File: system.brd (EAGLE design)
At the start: 52.4 x 77 mm, 122 parts, among them IC1 TPS7B8650BQDDARQ1, J1 OLED, J2 163-179PH-EX, J3 AD2, J4 MCU, SW1 1825910-6, SW2 1825910-6, SW3 1825910-6, U1 ATMEGA328PB-AU, Y1 ABL-16.000MHZ-B2

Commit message: routing
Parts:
- removed J3: AD2, RS1-02-G:CONN_RS1-02-G_ADM
- removed LDO:J1: RS1-02-G, RS1-02-G:CONN_RS1-02-G_ADM
- removed SW2, SW3: 1825910-6, 1825910-6:SW_1825910-6-4
- added 5V_BACKUP: 5010, 5010:5010
- added AD2_BG: AD2_BG, RS1-02-G:CONN_RS1-02-G_ADM
- added LDO:AD2_5V: RS1-02-G, RS1-02-G:CONN_RS1-02-G_ADM
- added SW_MCU_RST, SW_MISC1: 1825910-6, 1825910-6:SW_1825910-6-4
- added U$1, U$2, U$3, U$4: (no value), SparkFun-Hardware:STAND-OFF
- moved V_TH 61.8 mm to (48.8, 27.1)
- moved RST_ADC 48.8 mm to (42.3, -5.71)
- moved TP10 47.7 mm to (28.6, -6.10)
- moved SDA 40.1 mm to (22.9, -6.22)
- moved ADC:C1 38.1 mm to (45.2, -1.91)
- moved R18 38.0 mm to (49.1, -0.76)
- moved 1.5V 34.9 mm to (10.7, 33.1)
- moved C6 34.7 mm to (50.7, 2.03)
- moved ADC:R2 33.2 mm to (44.7, 2.29)
- moved L1 30.8 mm to (13.2, -3.56), flipped to the bottom
- moved MCU_RST 29.5 mm to (10.7, 27.1)
- moved ADC:IC1 29.3 mm to (39.2, -1.14)
- moved 5V 28.6 mm to (16.8, 42.3)
- moved 2.5V 28.2 mm to (17.1, 33.1)
- moved ADC:C2 26.9 mm to (33.4, 10.9)
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- renumbered SW1 to SW_START
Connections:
- net 0: now also AD2_BG.1, LDO:AD2_5V.2, SW_MCU_RST.1, SW_MISC1.1; no longer J3.1, LDO:J1.2, SW2.1, SW3.1
- net LDO:N$3: now also LDO:AD2_5V.1; no longer LDO:J1.1
- net MCU_RST: now also SW_MCU_RST.3; no longer SW3.3
- net N$11: now also AD2_BG.2; no longer J3.2
- net N$19: now also SW_MCU_RST.4, SW_MISC1.4; no longer SW2.4, SW3.4
- net PB_MISC1: now also SW_MISC1.3; no longer SW2.3
- net VS_5V_BACKUP: now also 5V_BACKUP.1
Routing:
- net VS_5V_OUT: track 31.6 -> 98.4 mm, vias 2 -> 4
- net MCU_RST: track 0.00 -> 46.5 mm, vias 0 -> 2
- net PB_START: track 0.00 -> 42.0 mm
- net BG:N$4: track 37.1 -> 11.0 mm, vias 2 -> 1
- net N$4: track 0.00 -> 25.3 mm
- net PB_MISC1: track 0.00 -> 23.2 mm
- net ADC:N$2: track 23.2 -> 0.00 mm, vias 2 -> 0
- net VS_1.5V_OUT: track 7.51 -> 25.8 mm, vias 0 -> 1
- net BK:N$2: track 32.8 -> 14.5 mm, vias 1 -> 0
- net SDA: track 0.00 -> 17.4 mm, vias 0 -> 2
- net ADC:N$4: track 17.0 -> 0.00 mm
- net V_SIG: track 16.9 -> 0.23 mm
- net N$5: track 16.4 -> 0.00 mm, vias 2 -> 0
- net MOSI_MCU: track 0.00 -> 13.9 mm
- net VS_9V: track 0.08 -> 12.9 mm
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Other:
- board size 52.4 x 77 mm -> 54.3 x 78.5 mm
- board text removed: "5V"
- board text removed: "BUCK IC"
- board text removed: "gnd"

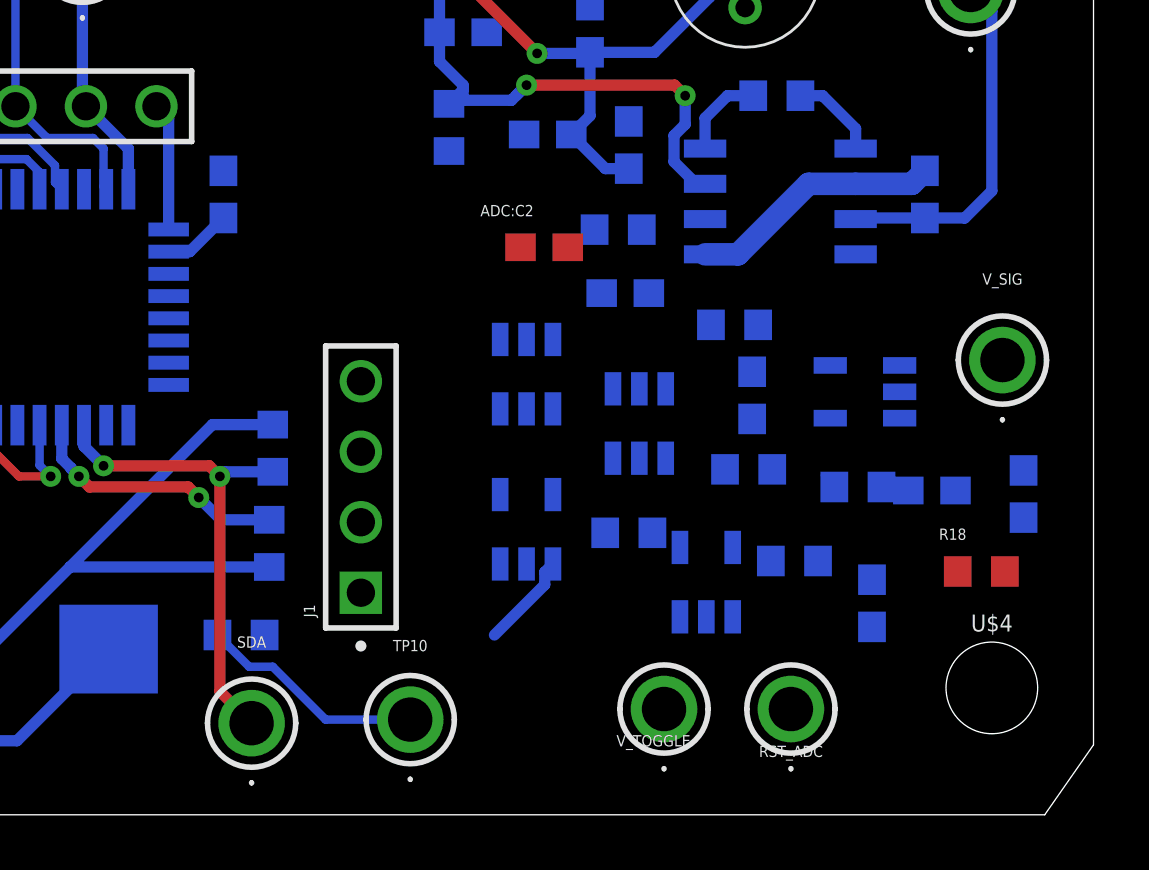
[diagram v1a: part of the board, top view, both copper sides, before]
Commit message: Rerouting ADC and AF
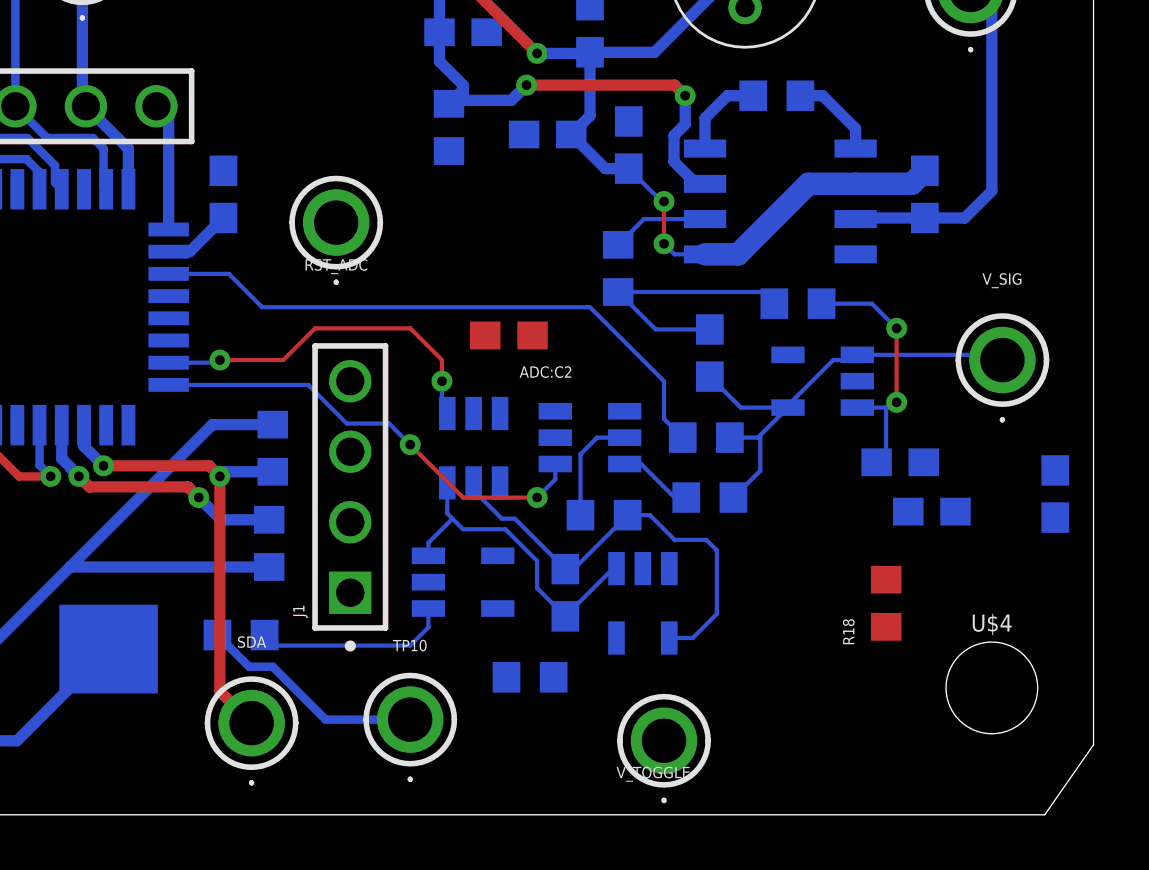
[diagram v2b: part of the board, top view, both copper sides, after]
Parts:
- moved RST_ADC 24.0 mm to (25.9, 11.8)
- moved ADC:R2 13.7 mm to (32.9, -4.57)
- moved AF:C8 11.6 mm to (46.2, 3.17)
- moved ADC:C1 11.1 mm to (34.2, -1.52)
- moved R16 3.81 mm to (39.4, 1.91)
- moved R18 3.61 mm to (45.7, -1.91), turned to 90 degrees
- moved ADC:C2 3.42 mm to (32.1, 7.75), turned to 0 degrees
- moved ADC:IC4 3.28 mm to (30.9, 3.68)
- moved ADC:IC2 2.98 mm to (30.5, -1.14), turned to 180 degrees
- moved AF:R5 2.41 mm to (42.5, 8.89)
- moved ADC:IC1 2.41 mm to (37.0, -1.91), turned to 270 degrees
- moved AF:C7 2.16 mm to (39.4, 7.11)
- moved R19 1.91 mm to (39.2, 4.06)
- moved ADC:IC5 1.85 mm to (35.1, 4.06), turned to 180 degrees
- moved AF:IC2 1.57 mm to (43.4, 6.10)
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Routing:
- net V_SIG_ADC: track 0.13 -> 21.9 mm
- net V_SIG: track 0.23 -> 17.1 mm
- net V_TOGGLE: track 0.00 -> 16.4 mm, vias 0 -> 2
- net ADC:N$4: track 0.00 -> 15.9 mm
- net RST_ADC: track 0.00 -> 12.8 mm, vias 0 -> 2
- net ADC:N$2: track 0.00 -> 11.7 mm
- net AF:N$6: track 0.21 -> 9.66 mm
- net AF:N$7: track 0.00 -> 9.35 mm, vias 0 -> 2
- net VS_2.5V_OUT: track 53.4 -> 58.3 mm, vias 3 -> 5
- net ADC:N$1: track 0.00 -> 4.04 mm
- net N$14: track 4.03 -> 7.61 mm
- net AF:N$3: track 0.54 -> 3.75 mm
- net N$2: track 0.00 -> 2.72 mm
- net N$6: track 0.54 -> 0.00 mm

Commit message: Update system.brd
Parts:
- moved BK:R2 0.76 mm to (27.1, 55.6)
- moved R23 0.68 mm to (36.4, 28.3)
- moved BK:C5 0.54 mm to (32.5, 54.1)
- moved BK:R5 0.54 mm to (32.5, 56.5)
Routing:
- net V_BG: track 31.9 -> 34.5 mm
- net BK:N$6: track 10.1 -> 11.1 mm
- net BK:N$5: track 5.90 -> 6.44 mm
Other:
- outline, holes or cut-outs redrawn

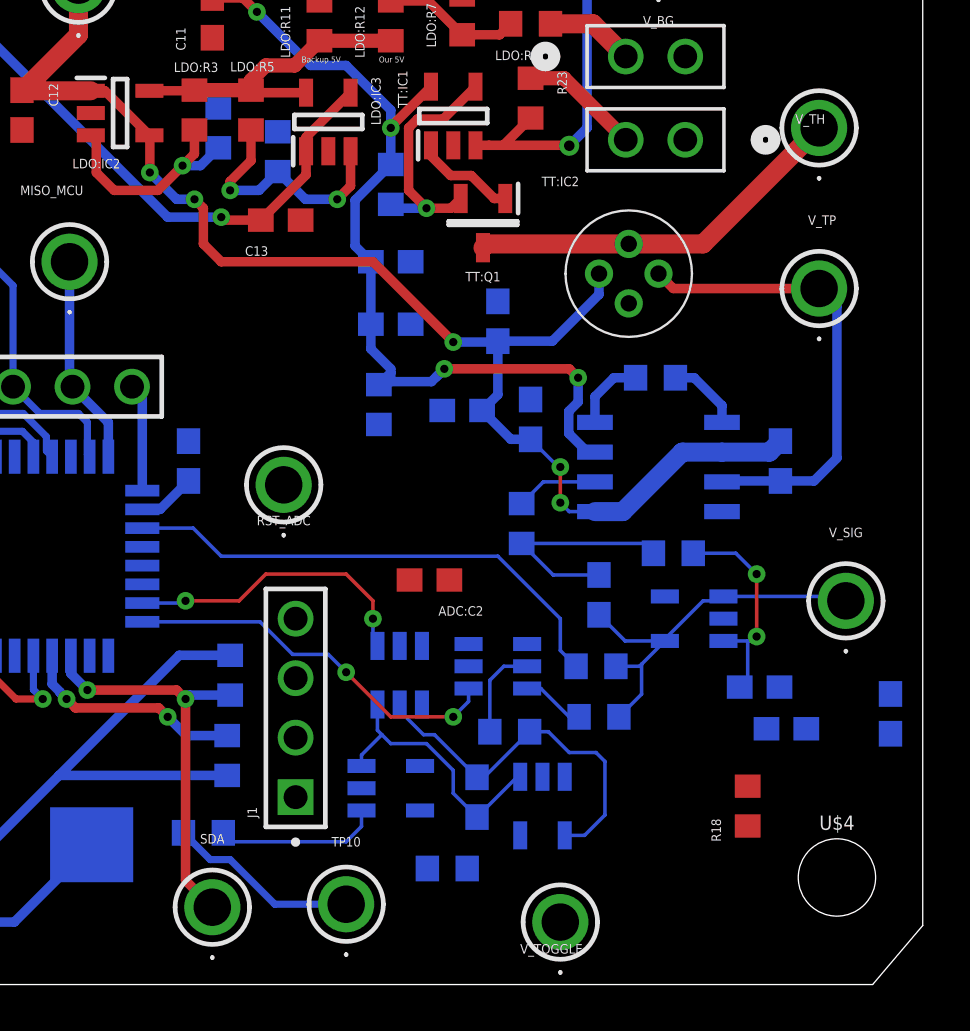
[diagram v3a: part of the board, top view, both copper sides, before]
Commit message: Wired Power lines to ADC and AF
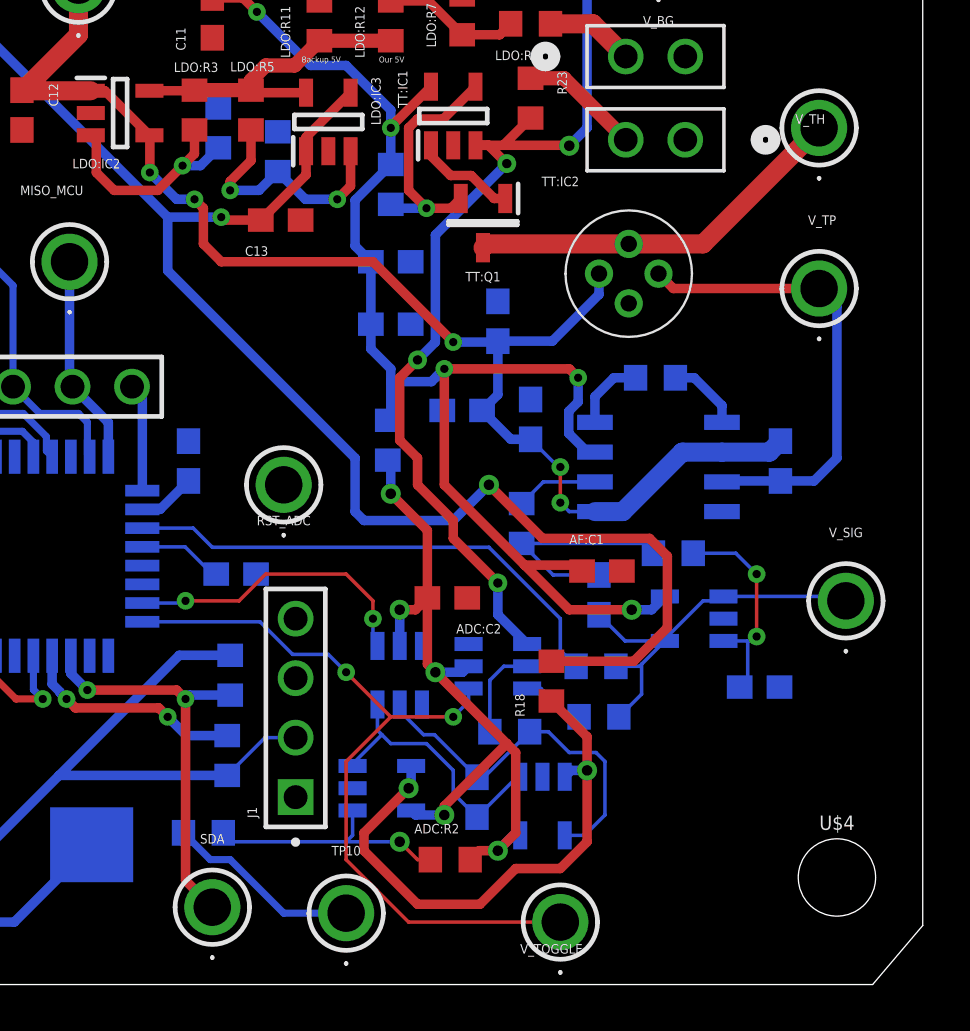
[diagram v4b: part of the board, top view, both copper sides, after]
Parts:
- moved C6 28.6 mm to (23.9, 8.00), turned to 180 degrees
- moved AF:C1 10.4 mm to (39.5, 8.13), flipped to the top, turned to 0 degrees
- moved R18 9.94 mm to (37.3, 3.43)
- moved R17 1.57 mm to (30.4, 13.7)
- moved ADC:C2 1.08 mm to (32.9, 6.99)
- moved ADC:R2 0.40 mm to (33.0, -4.19), flipped to the top, turned to 180 degrees
- moved ADC:IC2 0.38 mm to (30.1, -1.14)
- moved TP10 0.38 mm to (28.6, -6.48)
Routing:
- net VS_1.5V_OUT: track 25.8 -> 65.7 mm, vias 1 -> 2
- net N$6: track 0.00 -> 31.9 mm, vias 0 -> 5
- net V_BG: track 34.5 -> 60.8 mm, vias 2 -> 5
- net N$5: track 0.00 -> 23.7 mm, vias 0 -> 2
- net VS_5V_OUT: track 98.4 -> 122.0 mm, vias 4 -> 5
- net V_TOGGLE: track 16.4 -> 33.6 mm
- net N$15: track 0.00 -> 3.64 mm
- net N$14: track 7.61 -> 10.8 mm, vias 0 -> 1

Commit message: pcb
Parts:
- moved V_TOGGLE 3.14 mm to (40.8, -7.62)
- moved L1 2.08 mm to (11.9, -5.21), turned to 180 degrees
- moved ADC:IC1 2.05 mm to (38.9, -2.67)
- moved C6 1.82 mm to (25.7, 8.38), flipped to the top, turned to 0 degrees
- moved AVCC 1.52 mm to (2.29, 0.00)
- moved U$3 1.37 mm to (1.91, -7.24)
- moved C4 1.20 mm to (22.5, 13.8)
- moved SDA 1.14 mm to (22.9, -7.37)
- moved TP10 1.14 mm to (28.6, -7.62)
- moved TT:C1 1.05 mm to (29.5, 18.9)
- moved J1 1.02 mm to (26.4, 1.27)
- moved R16 0.90 mm to (40.3, 1.78)
- moved TT:Q1 0.81 mm to (34.9, 22.4)
- moved AF:IC2 0.64 mm to (44.1, 6.10)
- moved RST_ADC 0.63 mm to (26.4, 12.2)
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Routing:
- net V_TH: track 16.5 -> 49.0 mm, vias 0 -> 1
- net VS_5V_OUT: track 122.0 -> 145.5 mm, vias 5 -> 10
- net N$4: track 25.3 -> 12.0 mm
- net VS_1.5V_OUT: track 65.7 -> 52.3 mm, vias 2 -> 1
- net ADC_EXT_INT: track 8.37 -> 21.6 mm, vias 0 -> 2
- net SDA: track 17.4 -> 23.2 mm, vias 2 -> 1
- net V_TOGGLE: track 33.6 -> 39.2 mm
- net RST_ADC: track 12.8 -> 17.9 mm, vias 2 -> 1
- net SCL: track 9.61 -> 13.1 mm, vias 2 -> 0
- net N$5: track 23.7 -> 27.1 mm
- net BG:N$1: track 21.9 -> 18.6 mm
- net MCU_RST: track 46.5 -> 49.3 mm
- net N$6: track 31.9 -> 34.3 mm
- net ADC:N$4: track 15.9 -> 18.1 mm
- net VS_5V_BACKUP: track 31.7 -> 33.7 mm
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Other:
- board size 54.3 x 78.5 mm -> 54.3 x 80.8 mm

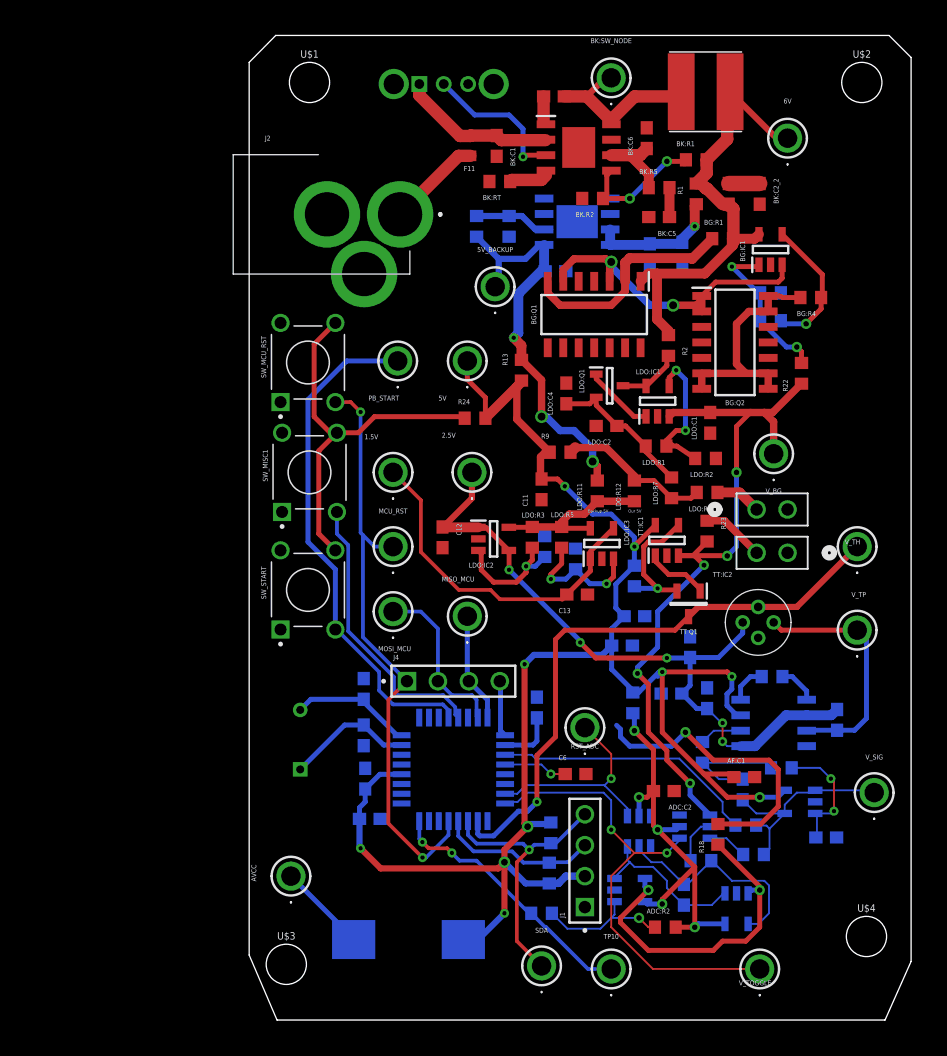
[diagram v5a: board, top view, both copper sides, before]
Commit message: finished routing: :q
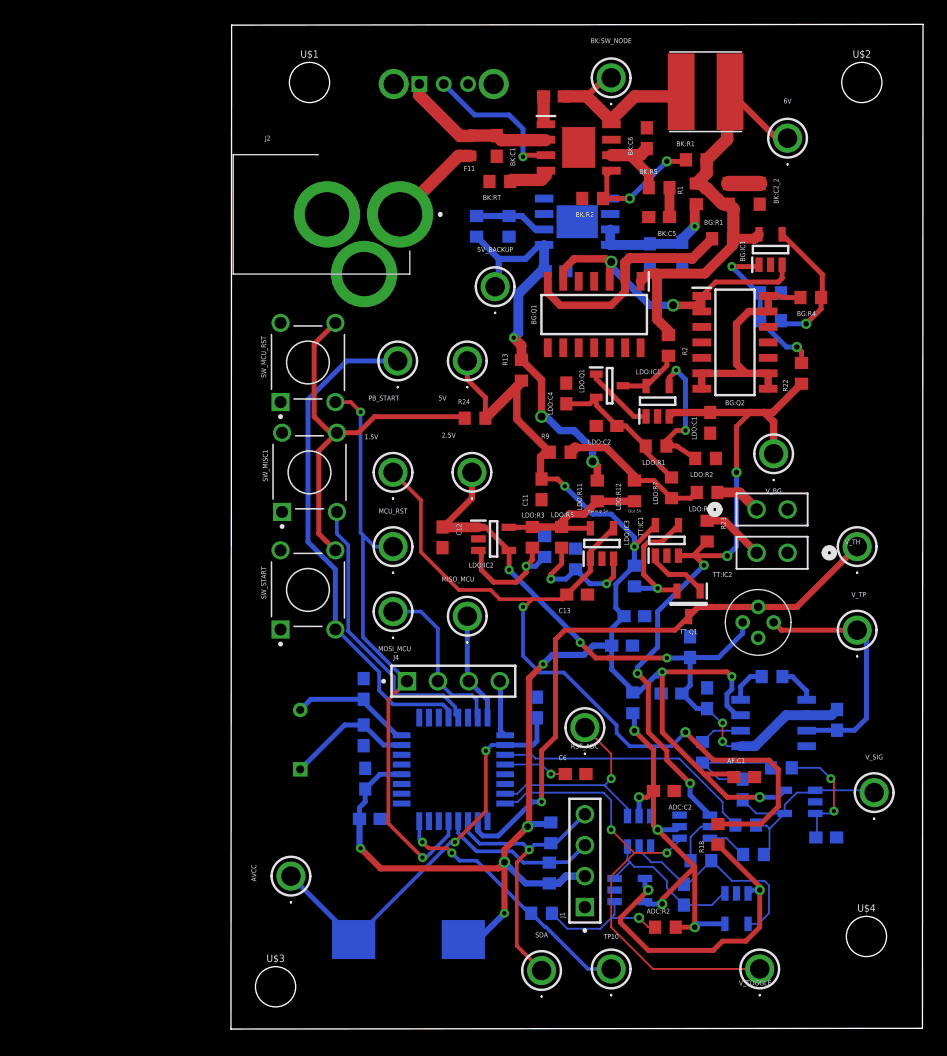
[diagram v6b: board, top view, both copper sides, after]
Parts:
- moved U$3 2.04 mm to (1.02, -9.08)
- moved SDA 0.38 mm to (22.9, -7.75)
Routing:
- net N$4: track 12.0 -> 34.0 mm, vias 0 -> 2
- net VS_1.5V_OUT: track 52.3 -> 67.4 mm, vias 1 -> 2
- net VS_5V_OUT: track 145.5 -> 144.4 mm
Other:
- board size 54.3 x 80.8 mm -> 56.8 x 82.5 mm

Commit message: pcb
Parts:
- moved U$4 2.95 mm to (48.3, -7.62)
- moved U$3 2.11 mm to (2.54, -7.62)
- moved L1 1.48 mm to (13.0, -6.27)
- moved U$1 1.28 mm to (2.57, 64.8)
- moved U$2 0.97 mm to (48.3, 64.8)
- moved R16 0.50 mm to (40.6, 1.38)
- moved V_SIG 0.37 mm to (49.8, 6.97)
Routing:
- net N$4: track 34.0 -> 38.3 mm
- net VS_1.5V_OUT: track 67.4 -> 68.0 mm
- net VS_6V: track 36.6 -> 36.0 mm
- net V_SIG: track 17.8 -> 17.3 mm
- added copper zone on layer 1, net 0
- added copper zone on layer 16, net 0
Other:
- board size 56.8 x 82.5 mm -> 55.9 x 82.5 mm
